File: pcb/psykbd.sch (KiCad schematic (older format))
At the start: 16 parts

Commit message: Assigning Footprints
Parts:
- C1, C2, C3, C4, C5, C6, C7: renamed from C?; footprint (none) -> Capacitor_SMD:C_0805_2012Metric_Pad1.15x1.40mm_HandSolder
- F1: renamed from F?; footprint (none) -> Fuse:Fuse_1206_3216Metric_Pad1.42x1.75mm_HandSolder
- R1, R2, R3, R4: renamed from R?; footprint (none) -> Keebio-Parts:R_0805
- SW1: renamed from SW?; footprint (none) -> kbd:ResetSW_1side
- USB1: renamed from USB?; footprint (none) -> random-keyboard-parts:Molex-0548190589
- Y1: renamed from Y?; footprint (none) -> Crystal:Crystal_SMD_3225-4Pin_3.2x2.5mm_HandSoldering
- gave numbers to parts that had none: 1
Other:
- moved on the sheet: C1, C2, C3, C4, C5, C6, C7, F1, R1, R2, R3, R4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

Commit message: Routing
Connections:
- net col0: now also U1.25 (PD4)
- net col1: now also U1.26 (PD6)
- net col10: now also U1.11 (PB3)
- net col11: now also U1.1 (PE6)
- net col2: now also U1.27 (PD7)
- net col3: now also U1.28 (PB4)
- net col4: now also U1.29 (PB5)
- net col5: now also U1.30 (PB6)
- net col6: now also U1.32 (PC7)
- net col7: now also U1.8 (PB0)
- net col8: now also U1.9 (PB1)
- net col9: now also U1.10 (PB2)
- net row0: now also U1.18 (PD0)
- net row1: now also U1.19 (PD1)
- net row2: now also U1.37 (PF6)
- net row3: now also U1.36 (PF7)
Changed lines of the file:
@@
 Wire Wire Line
 	3425 990  3425 900
-Connection ~ 3425 4590
-Connection ~ 3525 990
-Connection ~ 3425 990
-Wire Wire Line
-	3625 990  3525 990
-Wire Wire Line
-	3525 4590 3425 4590
-Wire Wire Line
-	3525 990  3425 990
 $Comp
 L power:GND #PWR0102
@@
 $EndComp
 $Comp
-L MCU_Microchip_ATmega:ATmega32U4-AU U1
-U 1 1 5E0DFF6A
-P 3525 2790
-F 0 "U1" H 3525 901 50  0000 C CNN
-F 1 "ATmega32U4-AU" H 3525 810 50  0000 C CNN
-F 2 "Package_QFP:TQFP-44_10x10mm_P0.8mm" H 3525 2790 50  0001 C CIN
-F 3 "http://ww1.microchip.com/downloads/en/DeviceDoc/Atmel-7766-8-bit-AVR-ATmega16U4-32U4_Datasheet.pdf" H 3525 2790 50  0001 C CNN
-	1    3525 2790
-	1    0    0    -1
-$EndComp
-Wire Wire Line
-	3090 4590 3425 4590
-$Comp
 L Device:R_Small R4
 U 1 1 5E0EAE60
@@
 	1    0    0    -1
 $EndComp
-Wire Wire Line
-	4125 3390 4325 3390
 Wire Wire Line
 	4525 3390 4890 3390
@@
 F1 "matrix.sch" 50
 $EndSheet
-Text GLabel 5605 1250 2    50   Input ~ 0
+Text GLabel 4260 3190 2    50   Input ~ 0
+col2
+Text GLabel 4260 1690 2    50   Input ~ 0
+col3
+Text GLabel 4255 1790 2    50   Input ~ 0
+col4
+Text GLabel 4250 1890 2    50   Input ~ 0
+col5
+Text GLabel 4250 2290 2    50   Input ~ 0
+col6
+Text GLabel 4225 1290 2    50   Input ~ 0
+col7
+Text GLabel 4225 1390 2    50   Input ~ 0
+col8
+Text GLabel 4230 1490 2    50   Input ~ 0
+col9
+Text GLabel 4230 1590 2    50   Input ~ 0
+col10
+Text GLabel 4265 4190 2    50   Input ~ 0
+row3
+Text GLabel 4265 4090 2    50   Input ~ 0
+row2
+Text GLabel 4230 2590 2    50   Input ~ 0
+row1
+Text GLabel 4230 2490 2    50   Input ~ 0
+row0
+Wire Wire Line
+	4125 1390 4225 1390
+Wire Wire Line
+	4125 1490 4230 1490
+Wire Wire Line
+	4125 1590 4230 1590
+Text GLabel 4260 2890 2    50   Input ~ 0
 col0
-Text GLabel 5630 1535 2    50   Input ~ 0
+Connection ~ 3425 4590
+Connection ~ 3525 990
+Connection ~ 3425 990
+Wire Wire Line
+	3625 990  3525 990
+Wire Wire Line
+	3525 990  3425 990
+Wire Wire Line
+	3525 4590 3425 4590
+Wire Wire Line
+	3090 4590 3425 4590
+Wire Wire Line
+	4265 4190 4125 4190
+Wire Wire Line
+	4265 4090 4125 4090
+Wire Wire Line
+	4125 3390 4325 3390
+Wire Wire Line
+	4125 2890 4260 2890
+Wire Wire Line
+	4125 2590 4230 2590
+Wire Wire Line
+	4230 2490 4125 2490
+Wire Wire Line
+	4250 2290 4125 2290
+Wire Wire Line
+	4125 1890 4250 1890
+Wire Wire Line
+	4125 1790 4255 1790
+Wire Wire Line
+	4125 1690 4260 1690
+Wire Wire Line
+	4260 3190 4125 3190
+$Comp
+L MCU_Microchip_ATmega:ATmega32U4-AU U1
+U 1 1 5E0DFF6A
+P 3525 2790
+F 0 "U1" H 3525 901 50  0000 C CNN
+F 1 "ATmega32U4-AU" H 3525 810 50  0000 C CNN
+F 2 "Package_QFP:TQFP-44_10x10mm_P0.8mm" H 3525 2790 50  0001 C CIN
+F 3 "http://ww1.microchip.com/downloads/en/DeviceDoc/Atmel-7766-8-bit-AVR-ATmega16U4-32U4_Datasheet.pdf" H 3525 2790 50  0001 C CNN
+	1    3525 2790
+	1    0    0    -1
+$EndComp
+Text GLabel 4265 3090 2    50   Input ~ 0
 col1
-Text GLabel 5550 1815 2    50   Input ~ 0
-col2
-Text GLabel 5460 2050 2    50   Input ~ 0
-col3
-Text GLabel 5385 2290 2    50   Input ~ 0
-col4
-Text GLabel 6125 1190 2    50   Input ~ 0
-col5
-Text GLabel 6160 1355 2    50   Input ~ 0
-col6
-Text GLabel 6165 1505 2    50   Input ~ 0
-col7
-Text GLabel 6155 1670 2    50   Input ~ 0
-col8
-Text GLabel 6135 1850 2    50   Input ~ 0
-col9
-Text GLabel 6145 2025 2    50   Input ~ 0
-col10
-Text GLabel 6175 2180 2    50   Input ~ 0
+Wire Wire Line
+	4265 3090 4125 3090
+Wire Wire Line
+	4225 1290 4125 1290
+Wire Wire Line
+	4125 3490 4230 3490
+Text GLabel 4230 3490 2    50   Input ~ 0
 col11
-Text GLabel 5645 3340 2    50   Input ~ 0
-row3
-Text GLabel 5645 3930 2    50   Input ~ 0
-row2
-Text GLabel 5635 4470 2    50   Input ~ 0
-row1
-Text GLabel 5615 5100 2    50   Input ~ 0
-row0
 $EndSCHEMATC

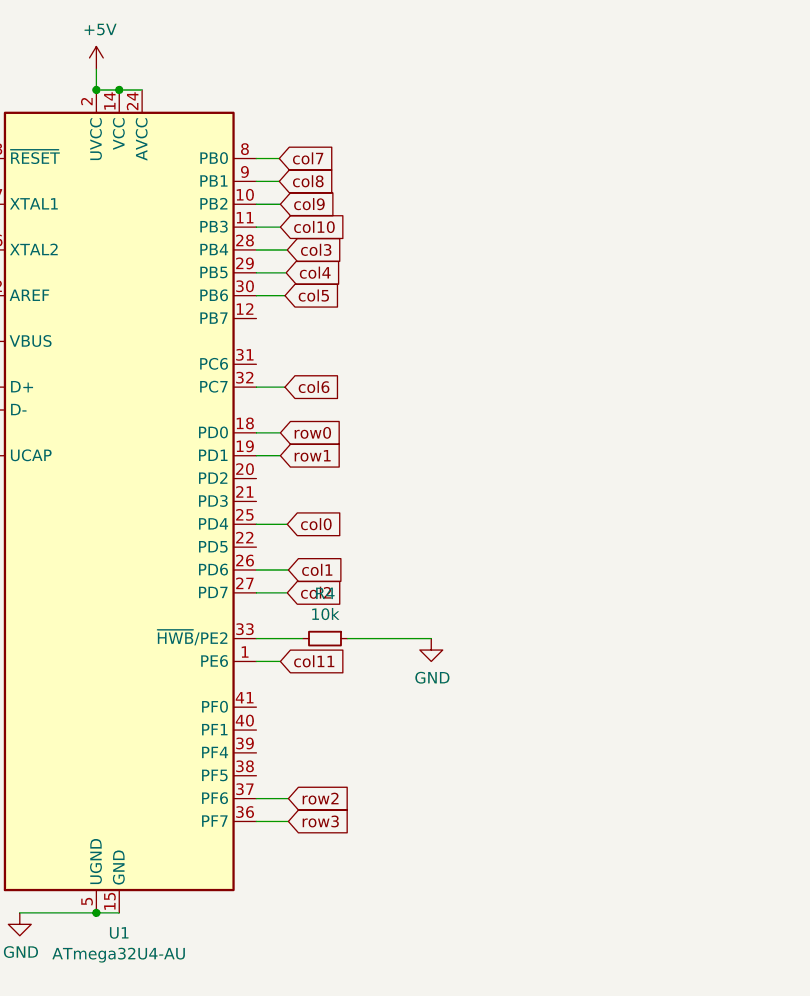
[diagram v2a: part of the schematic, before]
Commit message: chenge mcu position
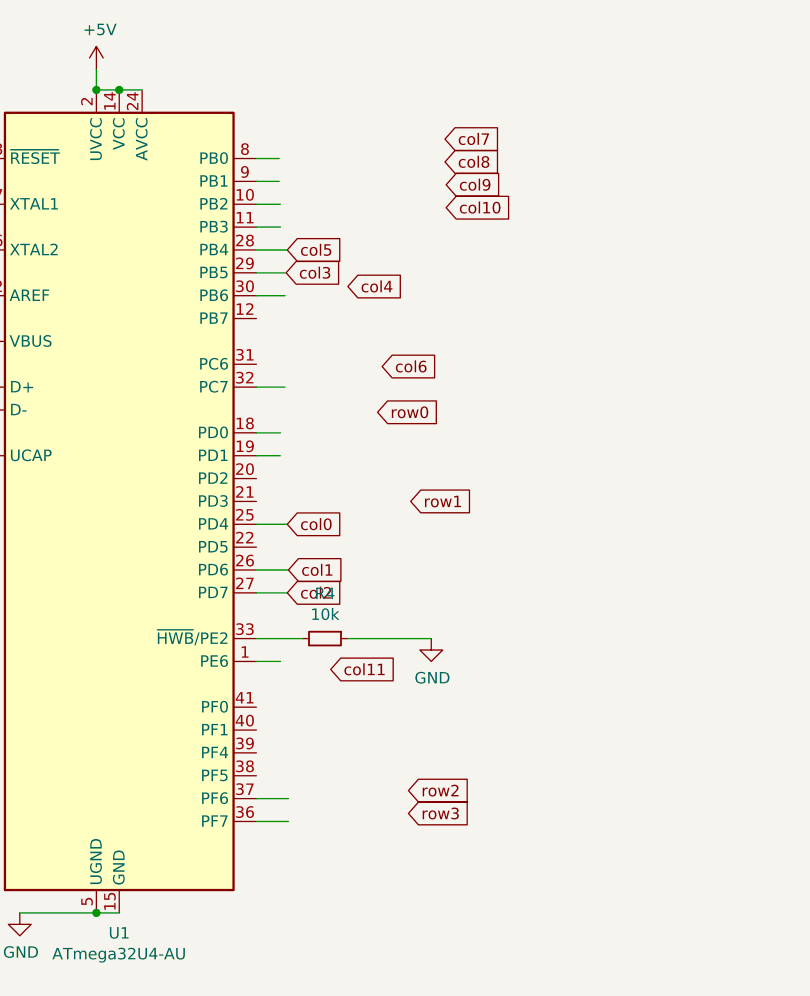
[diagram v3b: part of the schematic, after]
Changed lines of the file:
@@
 F1 "matrix.sch" 50
 $EndSheet
-Text GLabel 4260 3190 2    50   Input ~ 0
-col2
+Text GLabel 4255 1790 2    50   Input ~ 0
+col3
+Text GLabel 4525 1850 2    50   Input ~ 0
+col4
 Text GLabel 4260 1690 2    50   Input ~ 0
-col3
-Text GLabel 4255 1790 2    50   Input ~ 0
-col4
-Text GLabel 4250 1890 2    50   Input ~ 0
 col5
-Text GLabel 4250 2290 2    50   Input ~ 0
+Text GLabel 4675 2200 2    50   Input ~ 0
 col6
-Text GLabel 4225 1290 2    50   Input ~ 0
+Text GLabel 4950 1205 2    50   Input ~ 0
 col7
-Text GLabel 4225 1390 2    50   Input ~ 0
+Text GLabel 4950 1305 2    50   Input ~ 0
 col8
-Text GLabel 4230 1490 2    50   Input ~ 0
+Text GLabel 4955 1405 2    50   Input ~ 0
 col9
-Text GLabel 4230 1590 2    50   Input ~ 0
+Text GLabel 4955 1505 2    50   Input ~ 0
 col10
-Text GLabel 4265 4190 2    50   Input ~ 0
+Text GLabel 4790 4155 2    50   Input ~ 0
 row3
-Text GLabel 4265 4090 2    50   Input ~ 0
+Text GLabel 4790 4055 2    50   Input ~ 0
 row2
-Text GLabel 4230 2590 2    50   Input ~ 0
-row1
-Text GLabel 4230 2490 2    50   Input ~ 0
+Text GLabel 4655 2400 2    50   Input ~ 0
 row0
 Wire Wire Line
@@
 Wire Wire Line
 	4125 1590 4230 1590
-Text GLabel 4260 2890 2    50   Input ~ 0
-col0
 Connection ~ 3425 4590
 Connection ~ 3525 990
@@
 	1    0    0    -1
 $EndComp
-Text GLabel 4265 3090 2    50   Input ~ 0
-col1
 Wire Wire Line
 	4265 3090 4125 3090
@@
 Wire Wire Line
 	4125 3490 4230 3490
-Text GLabel 4230 3490 2    50   Input ~ 0
+Text GLabel 4450 3525 2    50   Input ~ 0
 col11
+Text GLabel 4265 3090 2    50   Input ~ 0
+col1
+Text GLabel 4260 2890 2    50   Input ~ 0
+col0
+Text GLabel 4800 2790 2    50   Input ~ 0
+row1
+Text GLabel 4260 3190 2    50   Input ~ 0
+col2
 $EndSCHEMATC

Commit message: before check
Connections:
- no-connect marks 0 -> 12
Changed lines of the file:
@@
 F1 "matrix.sch" 50
 $EndSheet
-Text GLabel 4255 1790 2    50   Input ~ 0
+Text GLabel 4225 2790 2    50   Input ~ 0
 col3
-Text GLabel 4525 1850 2    50   Input ~ 0
+Text GLabel 4230 2990 2    50   Input ~ 0
 col4
-Text GLabel 4260 1690 2    50   Input ~ 0
+Text GLabel 4230 1590 2    50   Input ~ 0
 col5
-Text GLabel 4675 2200 2    50   Input ~ 0
+Text GLabel 4265 4190 2    50   Input ~ 0
 col6
-Text GLabel 4950 1205 2    50   Input ~ 0
+Text GLabel 4265 4090 2    50   Input ~ 0
 col7
-Text GLabel 4950 1305 2    50   Input ~ 0
+Text GLabel 4265 3990 2    50   Input ~ 0
 col8
-Text GLabel 4955 1405 2    50   Input ~ 0
+Text GLabel 4275 3890 2    50   Input ~ 0
 col9
-Text GLabel 4955 1505 2    50   Input ~ 0
+Text GLabel 4275 3790 2    50   Input ~ 0
 col10
-Text GLabel 4790 4155 2    50   Input ~ 0
+Text GLabel 4260 2890 2    50   Input ~ 0
 row3
-Text GLabel 4790 4055 2    50   Input ~ 0
+Text GLabel 4250 1890 2    50   Input ~ 0
 row2
-Text GLabel 4655 2400 2    50   Input ~ 0
+Text GLabel 4230 1490 2    50   Input ~ 0
 row0
-Wire Wire Line
-	4125 1390 4225 1390
 Wire Wire Line
 	4125 1490 4230 1490
 Wire Wire Line
 	4125 1590 4230 1590
-Connection ~ 3425 4590
-Connection ~ 3525 990
-Connection ~ 3425 990
-Wire Wire Line
-	3625 990  3525 990
-Wire Wire Line
-	3525 990  3425 990
-Wire Wire Line
-	3525 4590 3425 4590
-Wire Wire Line
-	3090 4590 3425 4590
 Wire Wire Line
 	4265 4190 4125 4190
@@
 	4230 2490 4125 2490
 Wire Wire Line
-	4250 2290 4125 2290
-Wire Wire Line
 	4125 1890 4250 1890
 Wire Wire Line
-	4125 1790 4255 1790
+	4265 3090 4125 3090
+Text GLabel 4270 3690 2    50   Input ~ 0
+col11
+Text GLabel 4230 2590 2    50   Input ~ 0
+col1
+Text GLabel 4230 2490 2    50   Input ~ 0
+col0
+Text GLabel 4265 3090 2    50   Input ~ 0
+row1
+Text GLabel 4225 2690 2    50   Input ~ 0
+col2
 Wire Wire Line
-	4125 1690 4260 1690
+	4125 2690 4225 2690
 Wire Wire Line
-	4260 3190 4125 3190
+	4125 2790 4225 2790
+Wire Wire Line
+	4230 2990 4125 2990
+Wire Wire Line
+	4125 3690 4270 3690
+Wire Wire Line
+	4125 3790 4275 3790
+Wire Wire Line
+	4125 3890 4275 3890
+Wire Wire Line
+	4125 3990 4265 3990
+NoConn ~ 2925 1890
+NoConn ~ 4125 1990
+NoConn ~ 4125 2190
+NoConn ~ 4125 1290
+NoConn ~ 4125 1690
+NoConn ~ 4125 1790
+NoConn ~ 4125 2290
+NoConn ~ 4125 3190
+NoConn ~ 4125 3490
+Connection ~ 3425 4590
+Connection ~ 3525 990
+Connection ~ 3425 990
+Wire Wire Line
+	3625 990  3525 990
+Wire Wire Line
+	3525 990  3425 990
+Wire Wire Line
+	3525 4590 3425 4590
+Wire Wire Line
+	3090 4590 3425 4590
 $Comp
 L MCU_Microchip_ATmega:ATmega32U4-AU U1
@@
 	1    0    0    -1
 $EndComp
-Wire Wire Line
-	4265 3090 4125 3090
-Wire Wire Line
-	4225 1290 4125 1290
-Wire Wire Line
-	4125 3490 4230 3490
-Text GLabel 4450 3525 2    50   Input ~ 0
-col11
-Text GLabel 4265 3090 2    50   Input ~ 0
-col1
-Text GLabel 4260 2890 2    50   Input ~ 0
-col0
-Text GLabel 4800 2790 2    50   Input ~ 0
-row1
-Text GLabel 4260 3190 2    50   Input ~ 0
-col2
+NoConn ~ 4125 1390
+NoConn ~ 1460 4805
+NoConn ~ 1460 4405
 $EndSCHEMATC
